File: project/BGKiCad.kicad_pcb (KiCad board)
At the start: 2 copper layers, 63.5 x 50.8 mm, 2 parts, among them SW1 SW_choc_v1_HS_CPG135001S30_1u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

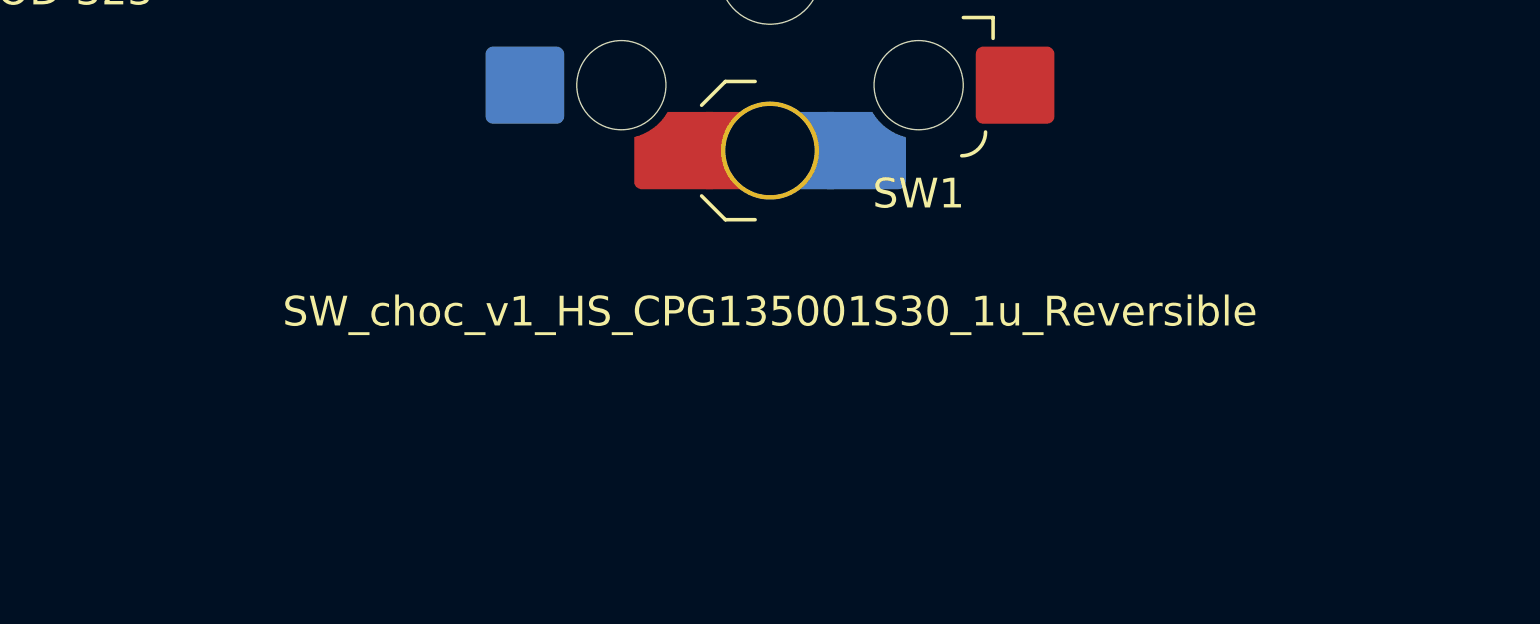
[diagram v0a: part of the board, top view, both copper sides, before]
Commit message: Change capitalization of footprint name
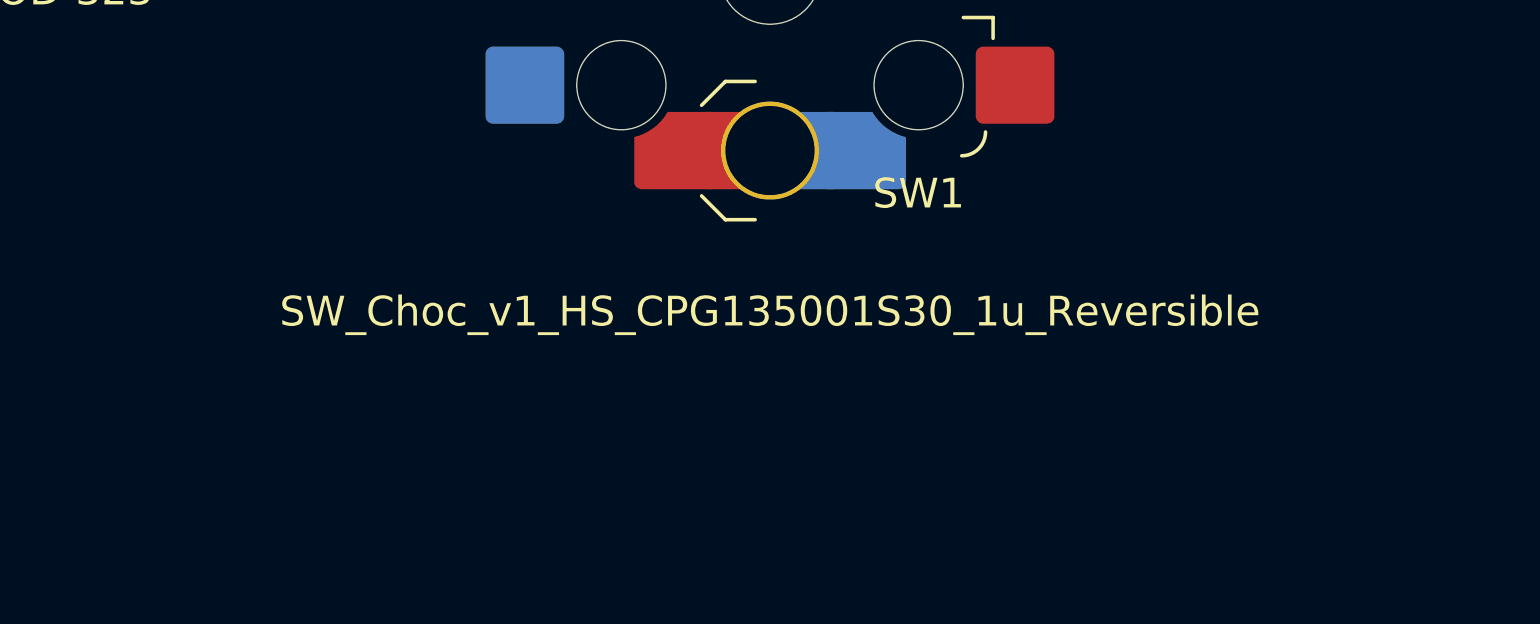
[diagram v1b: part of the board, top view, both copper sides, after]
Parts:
- SW1: value SW_choc_v1_HS_CPG135001S30_1u_Reversible -> SW_Choc_v1_HS_CPG135001S30_1u_Reversible; footprint BGKiCad:SW_choc_v1_HS_CPG135001S30_1u_Reversible -> BGKiCad:SW_Choc_v1_HS_CPG135001S30_1u_Reversible
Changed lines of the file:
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@@
 	(net 6 "unconnected-(SW1-Pad2)_3")
 	(net 7 "unconnected-(SW1-Pad2)_4")
-	(footprint "BGKiCad:SW_choc_v1_HS_CPG135001S30_1u_Reversible"
+	(footprint "BGKiCad:SW_Choc_v1_HS_CPG135001S30_1u_Reversible"
 		(layer "F.Cu")
 		(at 62.875 39.43)
@@
 			)
 		)
-		(property "Value" "SW_choc_v1_HS_CPG135001S30_1u_Reversible"
+		(property "Value" "SW_Choc_v1_HS_CPG135001S30_1u_Reversible"
 			(at 0 11.37 180)
 			(layer "F.SilkS")

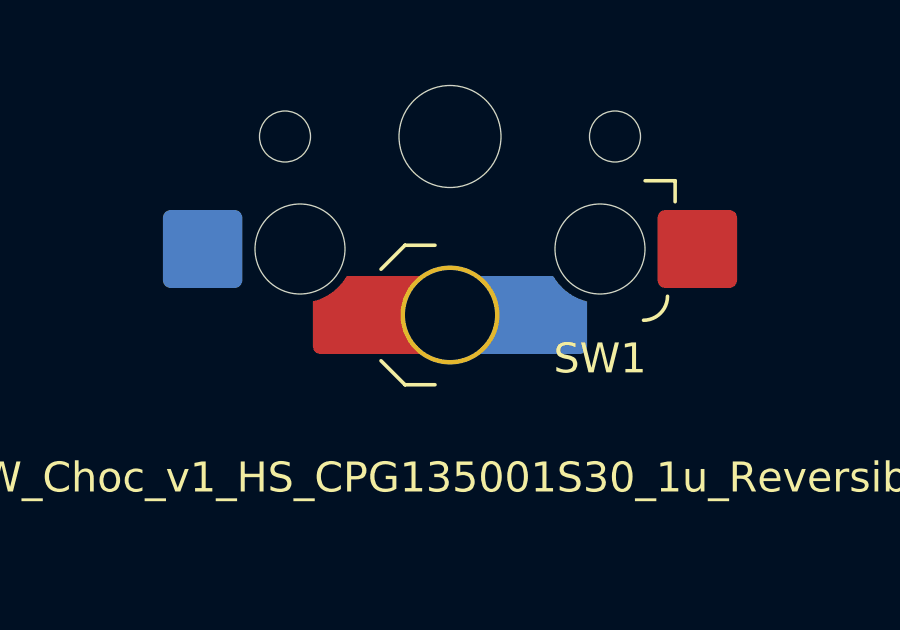
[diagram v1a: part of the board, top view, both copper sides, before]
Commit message: Tweak radius of pad 2 notch
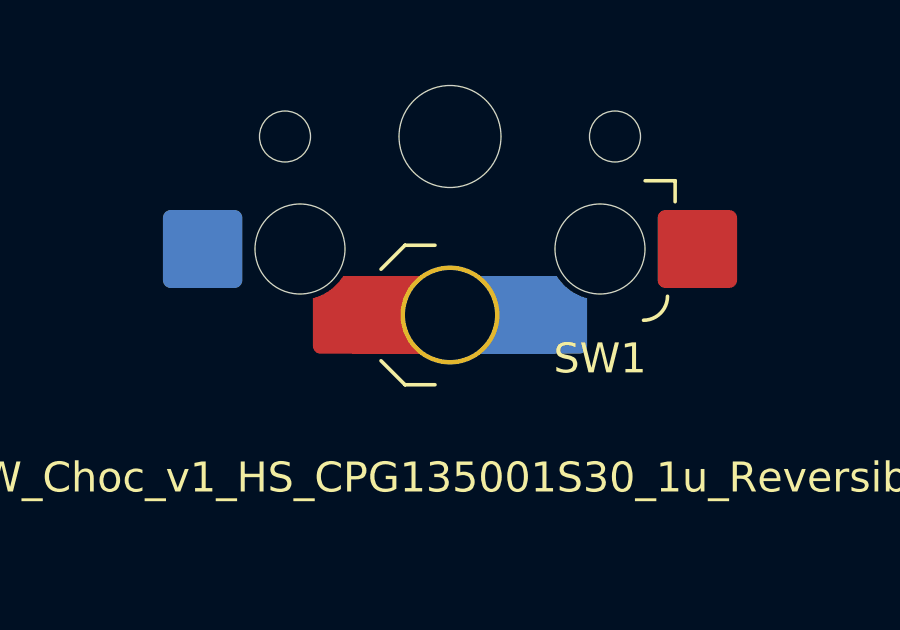
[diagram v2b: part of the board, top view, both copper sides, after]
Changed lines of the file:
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@@
 		(fp_line
 			(start -4.57 6.99)
-			(end -4.57 5.497884)
+			(end -4.57 5.394717)
 			(stroke
 				(width 0.05)
@@
 		(fp_line
 			(start -1.92 4.65)
-			(end -3.441155 4.65)
+			(end -3.557779 4.65)
 			(stroke
 				(width 0.05)
@@
 		)
 		(fp_arc
-			(start -3.441155 4.65)
-			(mid -3.727208 5.022792)
-			(end -4.57 5.497884)
+			(start -3.557779 4.65)
+			(mid -3.797918 4.952082)
+			(end -4.57 5.394717)
 			(stroke
 				(width 0.05)
@@
 			(size 1 1)
 			(layers "F.Cu" "F.Mask" "F.Paste")
-			(net 3 "unconnected-(SW1-Pad2)")
+			(net 5 "unconnected-(SW1-Pad2)_2")
 			(pinfunction "2")
 			(pintype "passive+no_connect")
@@
 					(pts
 						(arc
-							(start -1.325 -0.452116)
-							(mid -0.482208 -0.927208)
-							(end -0.196155 -1.3)
-						)
-						(xy 1.325 -1.3) (xy 1.325 1.3)
-						(arc
-							(start -1.065 1.3)
-							(mid -1.248848 1.223848)
-							(end -1.325 1.04)
-						)
+							(start -1.066079 1.290075)
+							(mid -1.249229 1.213543)
+							(end -1.325 1.030077)
+						)
+						(arc
+							(start -1.325 -0.555282)
+							(mid -0.552918 -0.997918)
+							(end -0.312778 -1.300001)
+						)
+						(xy 1.325 -1.300001) (xy 1.325 1.299999)
 					)
 					(width 0)
@@
 			(size 1.2 2.6)
 			(layers "F.Cu")
-			(net 4 "unconnected-(SW1-Pad2)_1")
+			(net 7 "unconnected-(SW1-Pad2)_4")
 			(pinfunction "2")
 			(pintype "passive+no_connect")
@@
 			(layers "*.Cu" "F.Mask")
 			(remove_unused_layers no)
-			(net 5 "unconnected-(SW1-Pad2)_2")
+			(net 6 "unconnected-(SW1-Pad2)_3")
 			(pinfunction "2")
 			(pintype "passive+no_connect")
@@
 			(size 1.2 2.6)
 			(layers "B.Cu")
-			(net 6 "unconnected-(SW1-Pad2)_3")
+			(net 3 "unconnected-(SW1-Pad2)")
 			(pinfunction "2")
 			(pintype "passive+no_connect")
@@
 			(size 1 1)
 			(layers "B.Cu" "B.Mask" "B.Paste")
-			(net 7 "unconnected-(SW1-Pad2)_4")
+			(net 4 "unconnected-(SW1-Pad2)_1")
 			(pinfunction "2")
 			(pintype "passive+no_connect")
@@
 					(pts
 						(arc
-							(start 1.325 -0.452116)
-							(mid 0.482208 -0.927208)
-							(end 0.196155 -1.3)
-						)
-						(xy -1.325 -1.3) (xy -1.325 1.3)
-						(arc
-							(start 1.065 1.3)
-							(mid 1.248848 1.223848)
-							(end 1.325 1.04)
-						)
+							(start 1.066079 1.290075)
+							(mid 1.249229 1.213543)
+							(end 1.325 1.030077)
+						)
+						(arc
+							(start 1.325 -0.555282)
+							(mid 0.552918 -0.997918)
+							(end 0.312778 -1.300001)
+						)
+						(xy -1.325 -1.300001) (xy -1.325 1.299999)
 					)
 					(width 0)
@@
 		(model "../3dmodels/HS_CPG135001S30_Choc.step"
 			(offset
-				(xyz -5 -3.75 0.12)
+				(xyz -5 -3.75 0.13)
 			)
 			(scale
@@
 			)
 			(rotate
-				(xyz 90 0 180)
-			)
-		)
+				(xyz 90 -0 180)
+			)
+		)

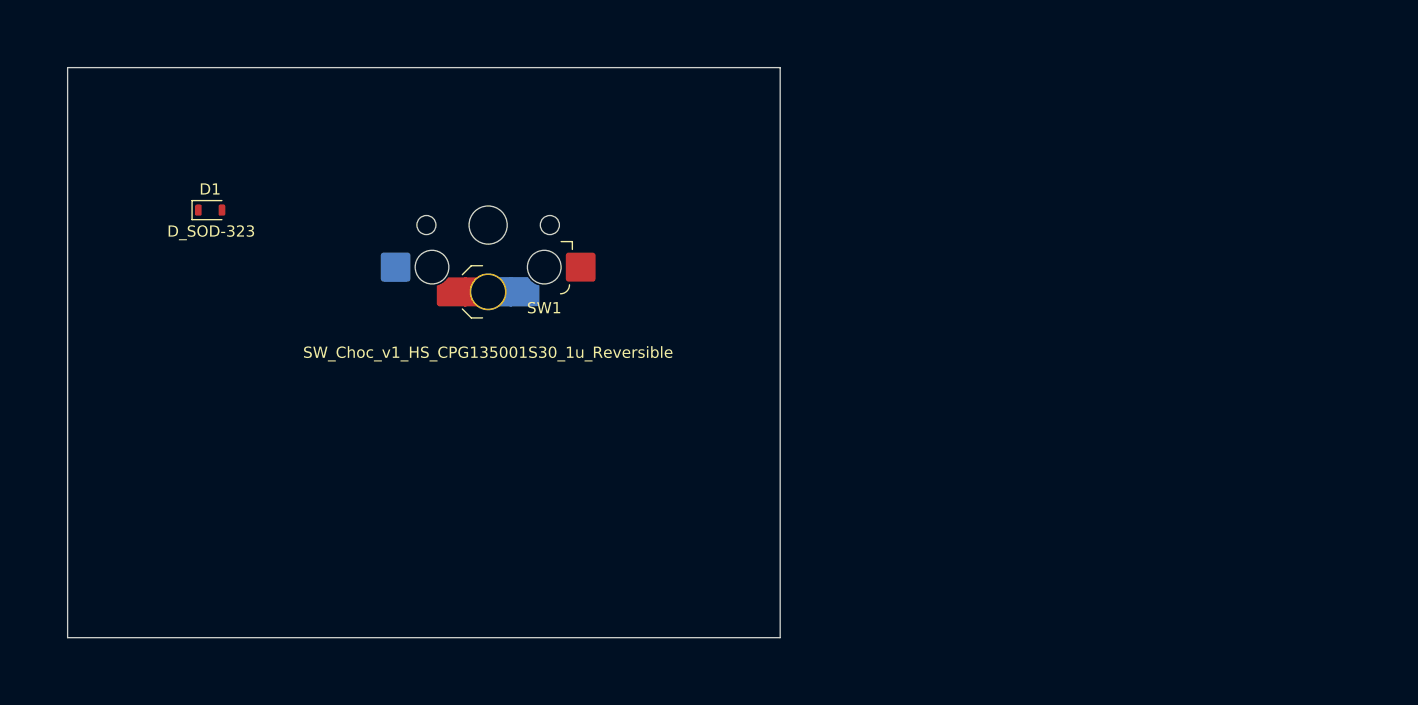
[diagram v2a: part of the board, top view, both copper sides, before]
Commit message: Add 1¼U and 1½U versions of Choc footprint
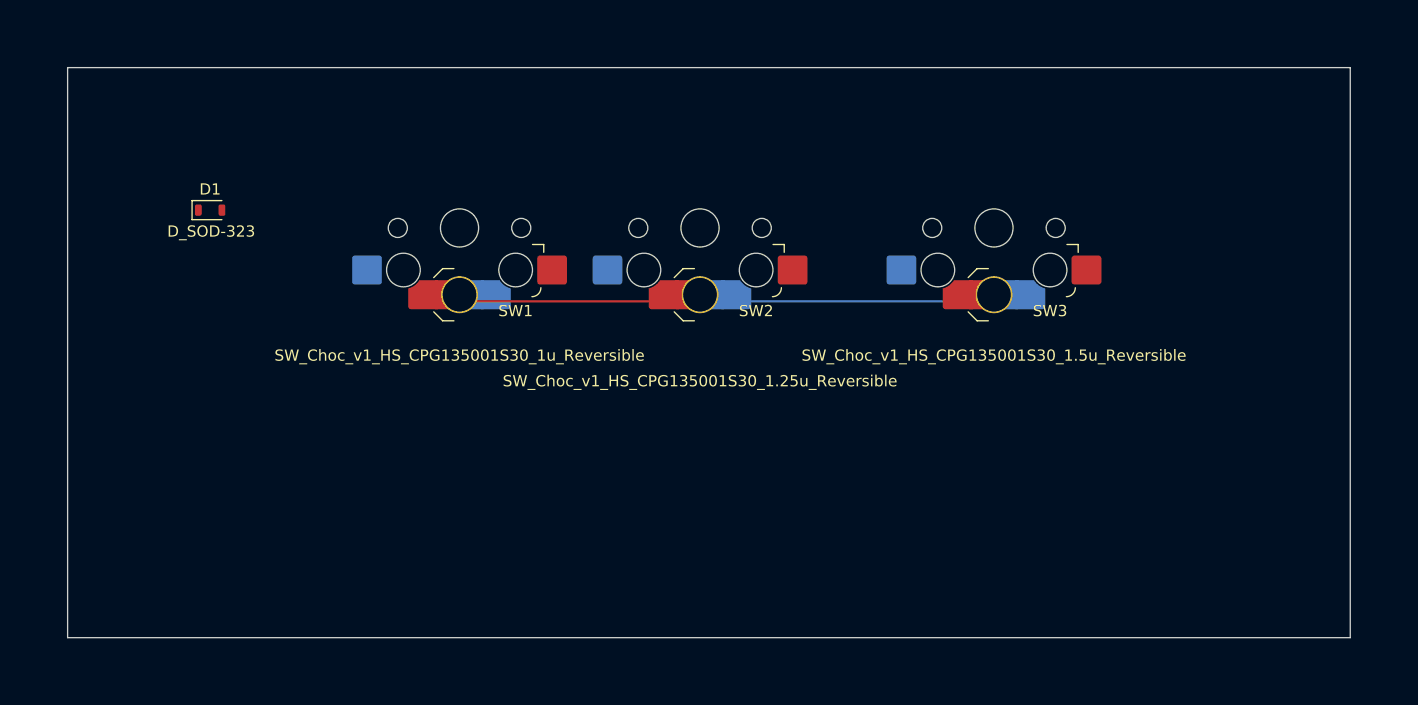
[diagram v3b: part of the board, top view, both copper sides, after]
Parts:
- added SW2: SW_Choc_v1_HS_CPG135001S30_1.25u_Reversible, BGKiCad:SW_Choc_v1_HS_CPG135001S30_1.25u_Reversible, F.Cu at (81.8, 39.7)
- added SW3: SW_Choc_v1_HS_CPG135001S30_1.5u_Reversible, BGKiCad:SW_Choc_v1_HS_CPG135001S30_1.5u_Reversible, F.Cu at (108.0, 39.7)
- moved SW1 2.56 mm to (60.3, 39.7)
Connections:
- SW1 pad 2: unconnected-(SW1-Pad2)_1 -> Net-(SW1-Pad2)
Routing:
- net Net-(SW1-Pad2): track 0.00 -> 48.6 mm
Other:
- board size 63.5 x 50.8 mm -> 114.3 x 50.8 mm

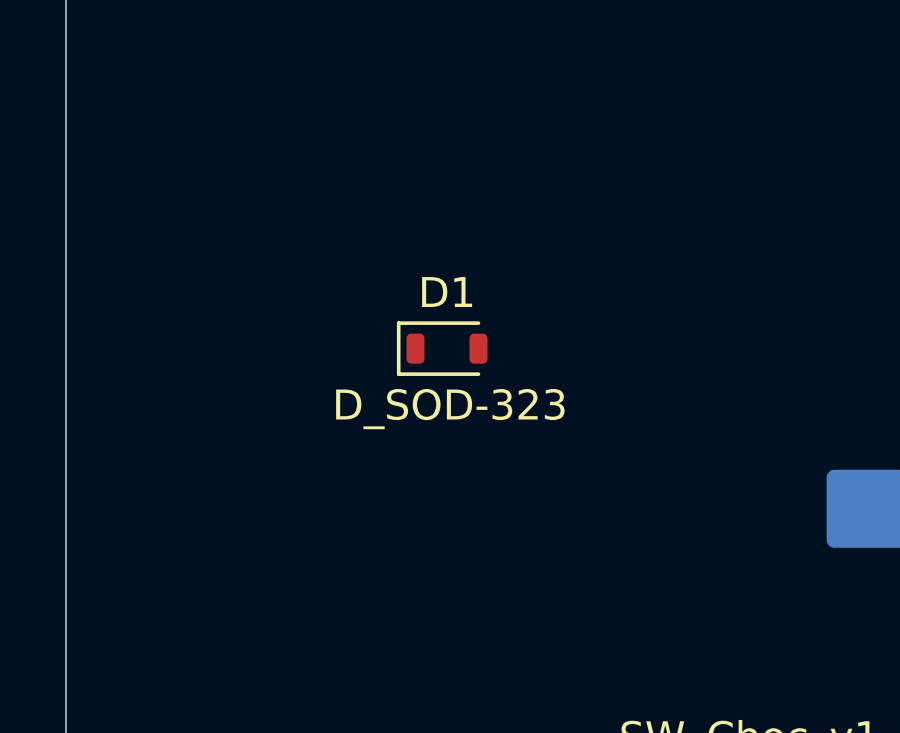
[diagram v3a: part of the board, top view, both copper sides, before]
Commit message: Add resistor to sample project
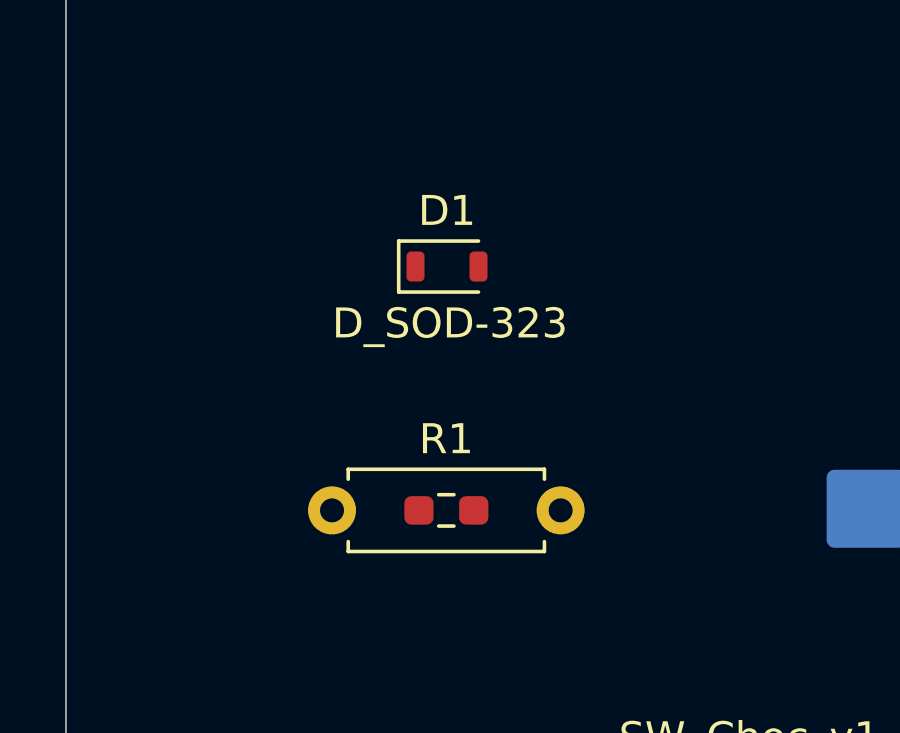
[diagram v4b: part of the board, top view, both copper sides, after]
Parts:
- added R1: R_Combined, BGK_Kicad:R_Combined_Axial_DIN0207_0603_1608Metric, F.Cu at (34.3, 43.5)
- moved D1 2.74 mm to (38.1, 35.4)

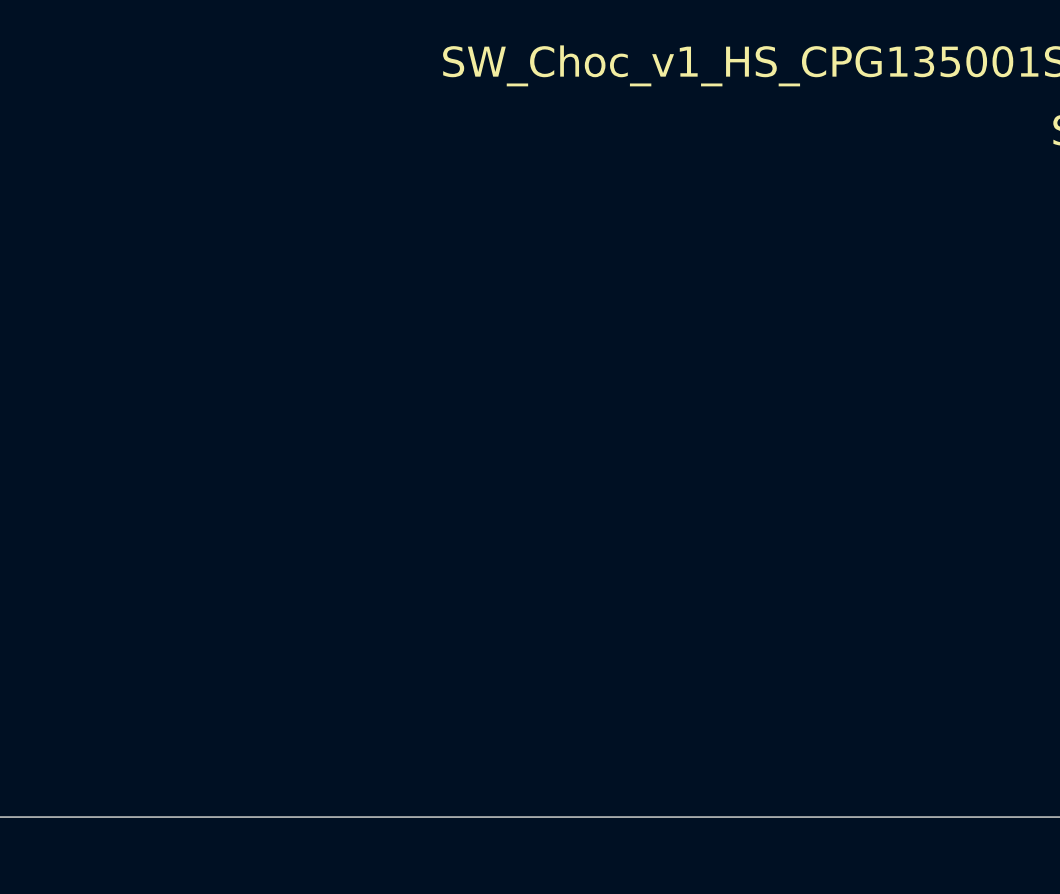
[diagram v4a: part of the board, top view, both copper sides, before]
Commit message: Add test point footprints to README and sample project
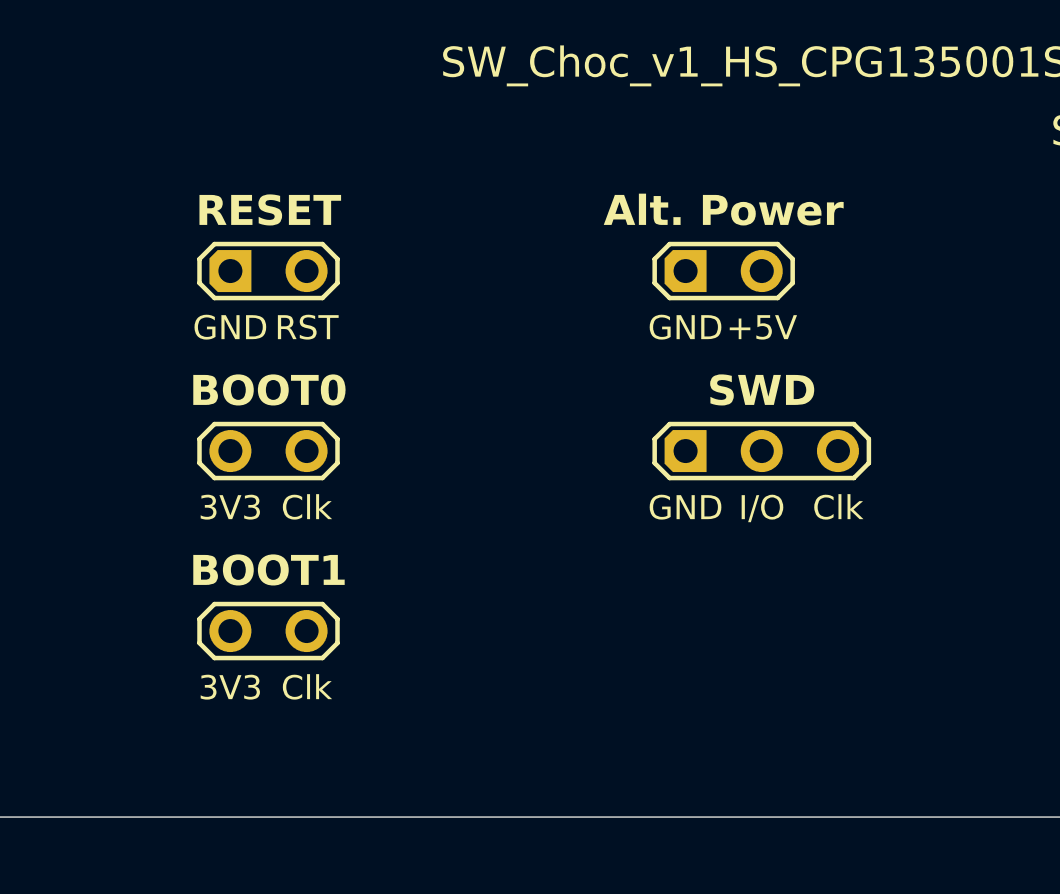
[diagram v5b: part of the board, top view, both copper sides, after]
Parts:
- added J1: Alt. Power, BGK_Kicad:TestPoint_2LabelledPads_Pitch2.54mm_Drill0.8mm, F.Cu at (52.0, 58.0)
- added J2: SWD, BGK_Kicad:TestPoint_3LabelledPads_Pitch2.54mm_Drill0.8mm, F.Cu at (52.0, 64.0)
- added TP1: RESET, BGK_Kicad:ResetJumper_Pitch2.54mm_Drill0.8mm, F.Cu at (36.8, 58.0)
- added TP2: BOOT0, BGKiCad:BootJumper_Pitch2.54mm_Drill0.8mm, F.Cu at (36.8, 64.0)
- added TP3: BOOT1, BGKiCad:BootJumper_Alt_Pitch2.54mm_Drill0.8mm, F.Cu at (36.8, 70.0)
